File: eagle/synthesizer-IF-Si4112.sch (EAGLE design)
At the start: 34 parts, among them J1 142-0701-851, J3 142-0701-851, U1 SI4112, X1 ECS-TXO-3225

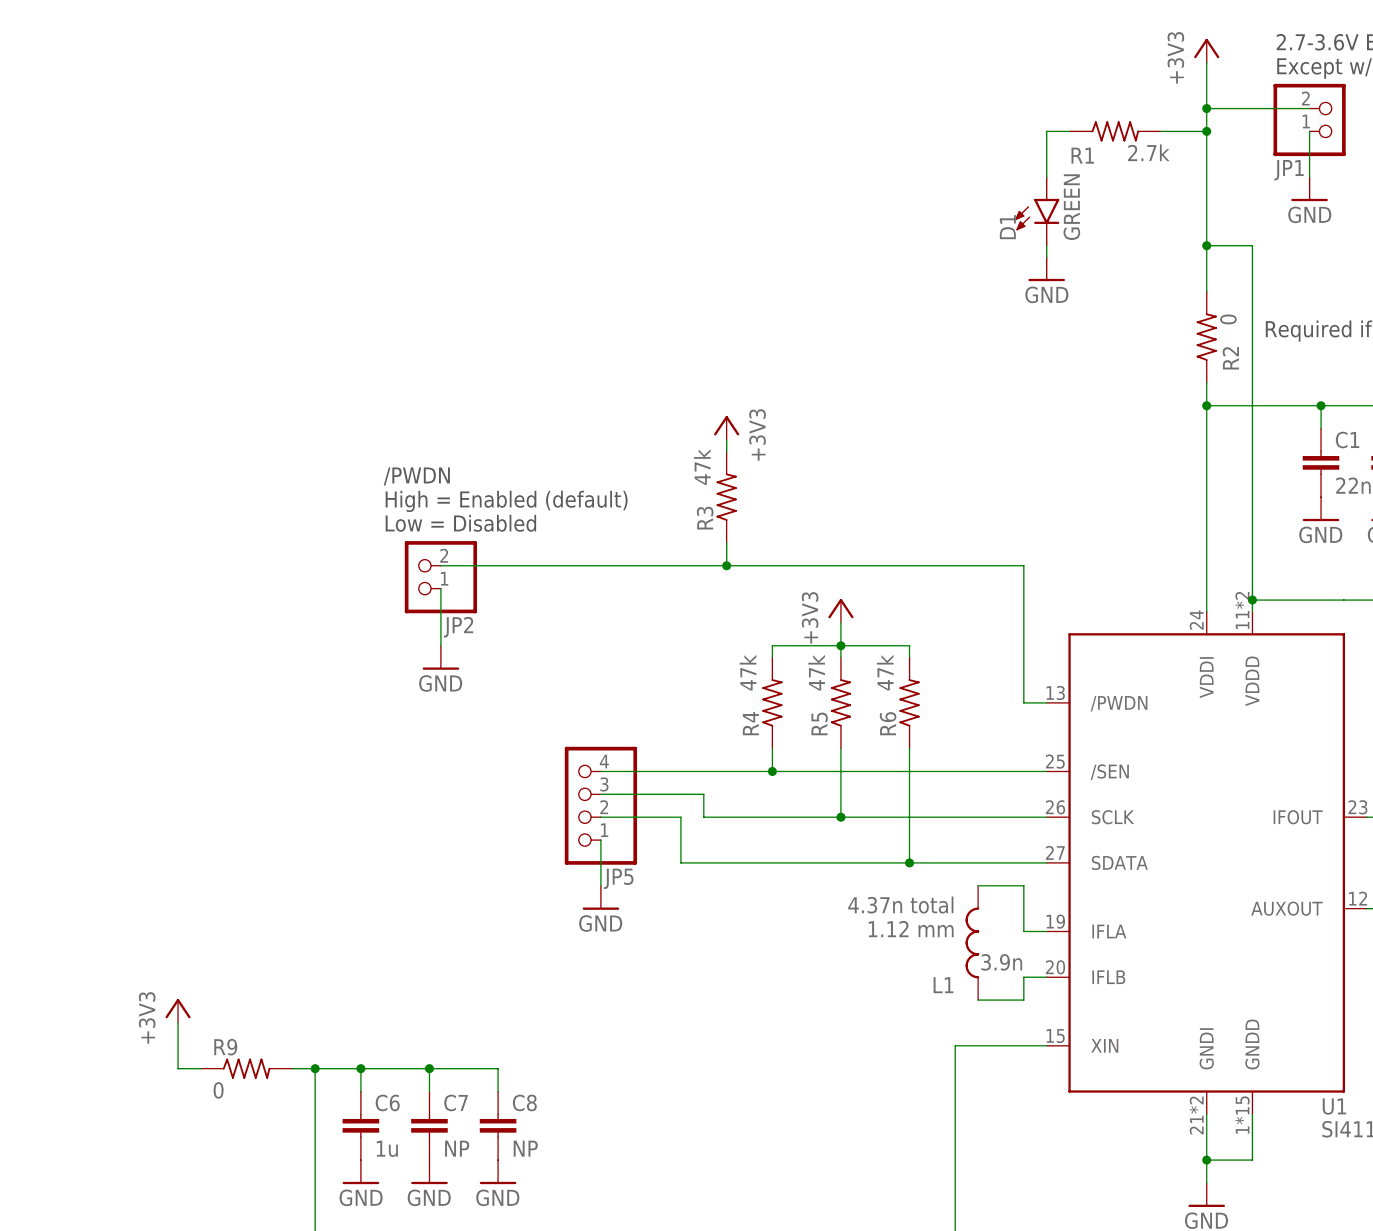
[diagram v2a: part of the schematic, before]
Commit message: Si4112, added better shutdown control
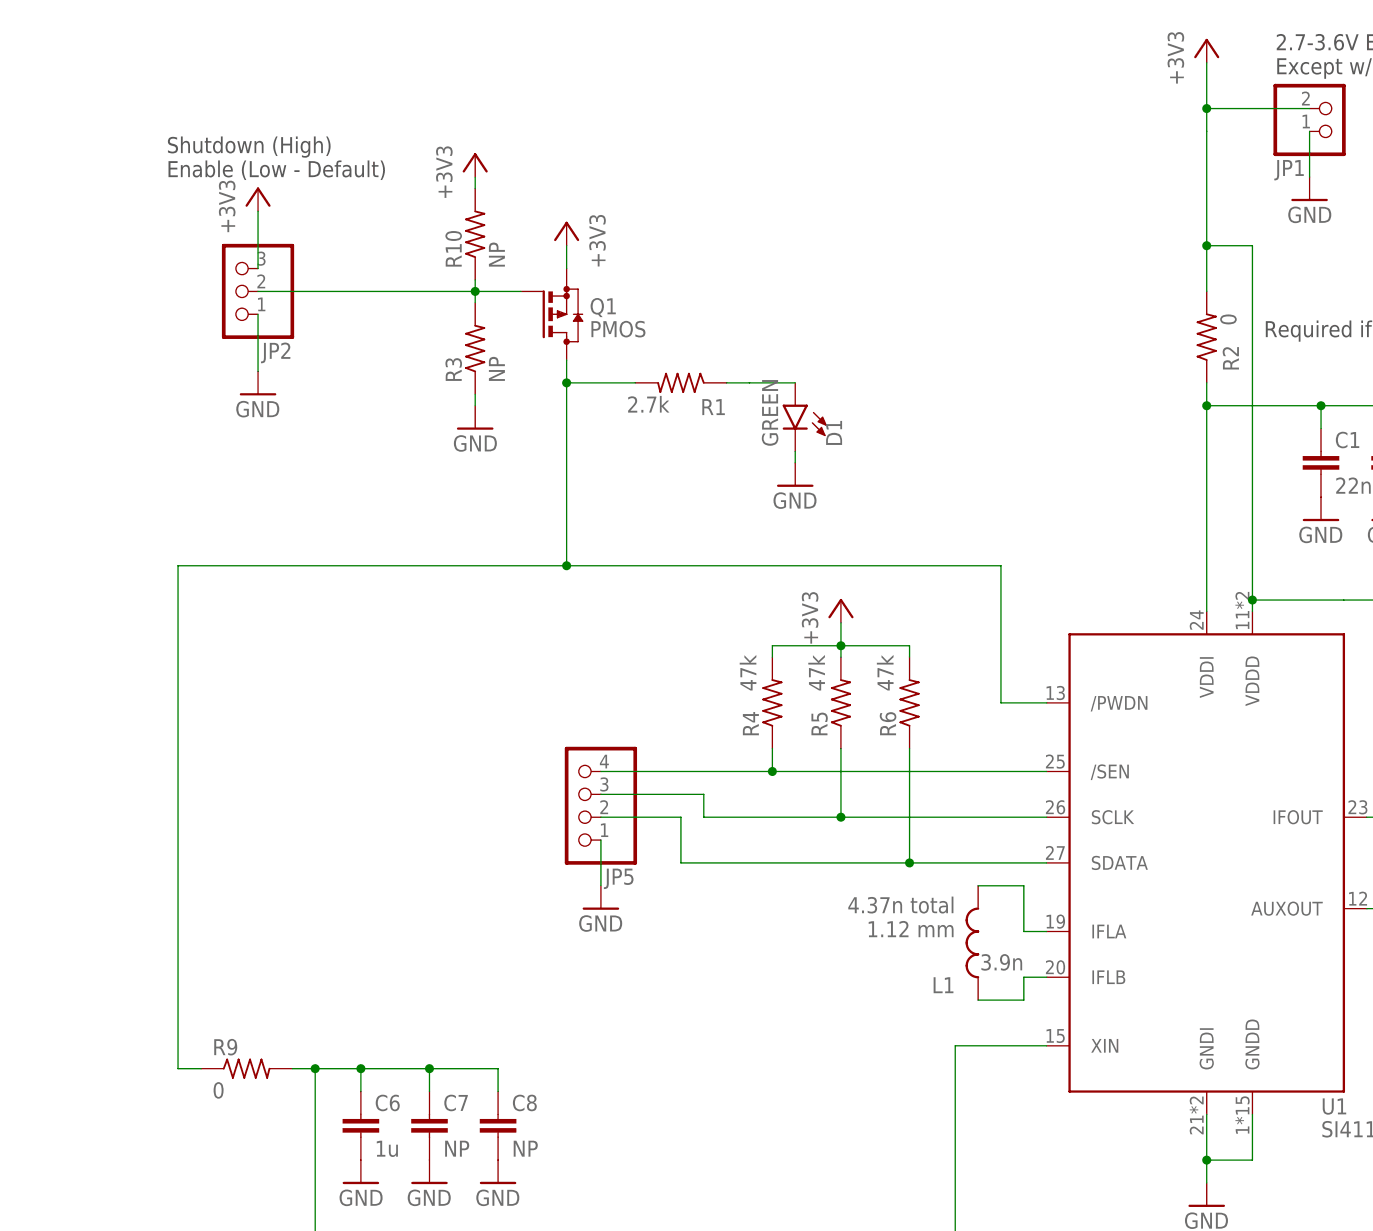
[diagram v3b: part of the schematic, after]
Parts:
- added Q1: PMOS, transistor-small-signal:BSS84
- added R10: NP, oresat-rcl:R-US_0402-B-NOSILK
- JP2: device pinhead:PINHD-1X2 -> pinhead:PINHD-1X3
- R3: value 47k -> NP
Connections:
- removed net /PWDN: JP2.2, R3.1, U1./PWDN
- new net N$4: JP2.2, Q1.G, R10.1, R3.2
- new net N$5: Q1.D, R1.2, R9.1, U1./PWDN
- net +3V3: now also JP2.3, Q1.S, R10.2; no longer R1.2, R3.2, R9.1
- net GND: now also R3.1
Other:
- note added: "Shutdown (High) Enable (Low - Default)"
- note removed: "/PWDN High = Enabled (default) Low = Disabled"
- moved on the sheet: D1, R1, R3

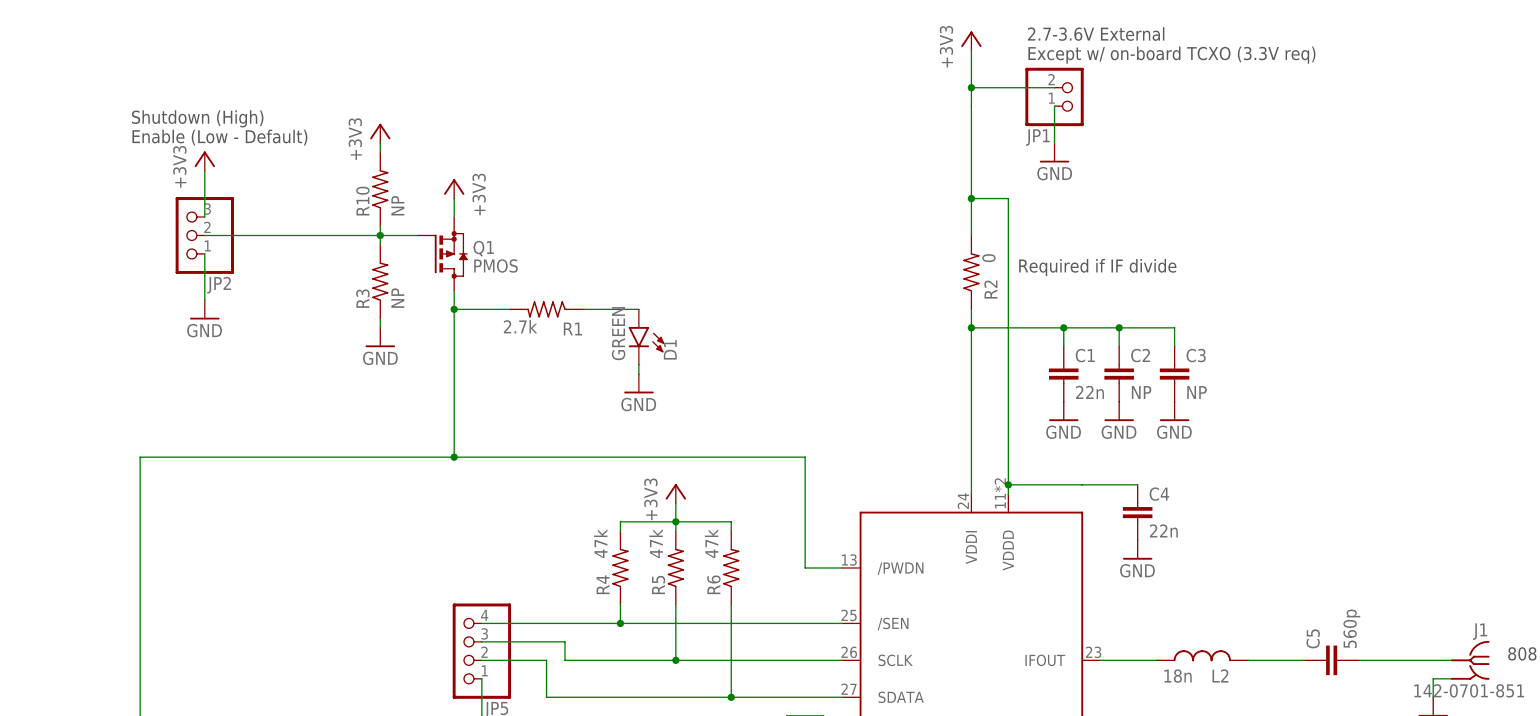
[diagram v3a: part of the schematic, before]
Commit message: Si4112, fix shutdown control and add bkup power down battery option
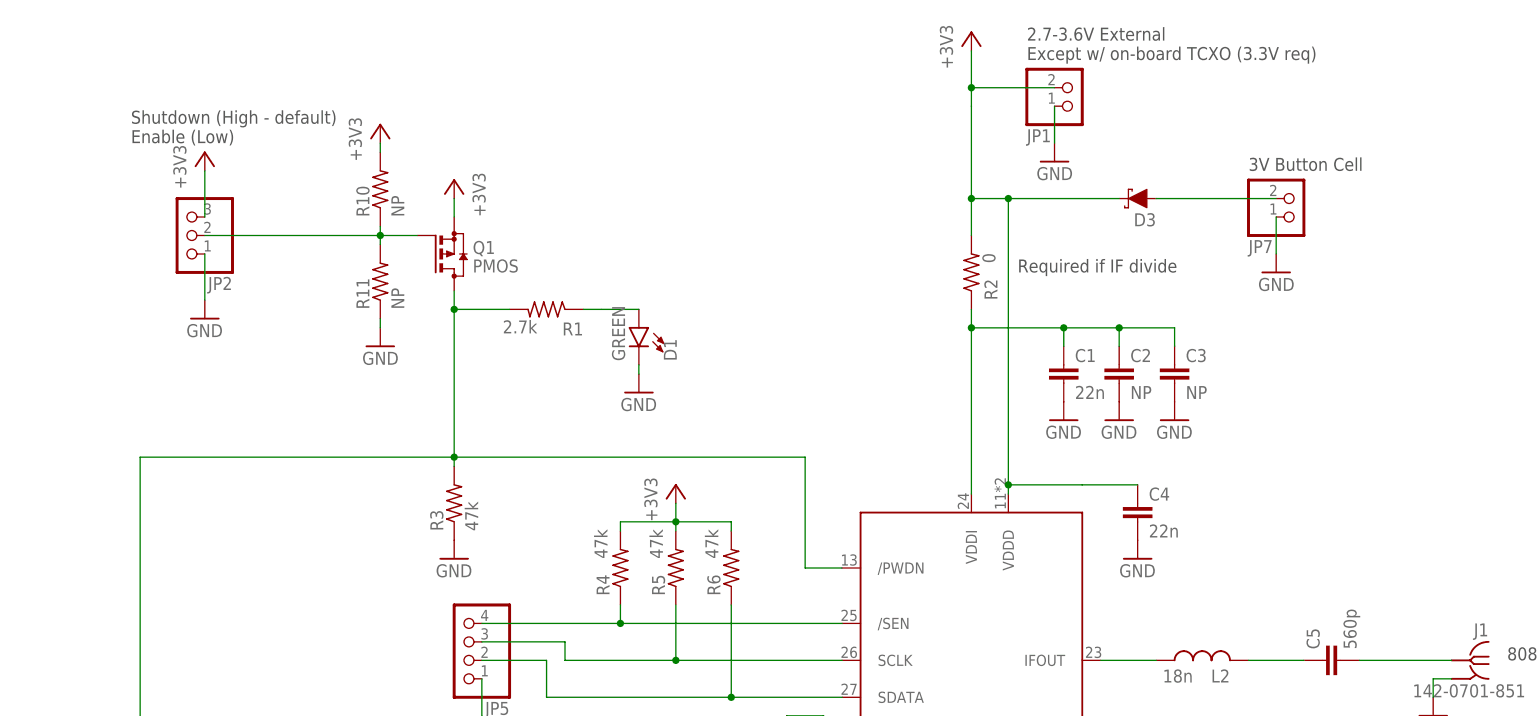
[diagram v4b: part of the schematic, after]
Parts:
- added D3: 120mA/40V/370mV, SparkFun-DiscreteSemi:DIODE-SCHOTTKY-RB751S40
- added JP7: (no value), pinhead:PINHD-1X2
- added R99: NP, oresat-rcl:R-US_0402-B-NOSILK
- R3: value NP -> 47k
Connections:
- new net N$1: D3.A, JP7.2
- net +3V3: now also D3.C
- net GND: now also JP7.1, R11.1
- net N$4: now also R11.2; no longer R3.2
- net N$5: now also R3.2
- net REF_IN: now also R99.2; no longer R11.2
- net XIN: now also R99.1; no longer R11.1
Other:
- note added: "3V Button Cell"
- note added: "Shutdown (High - default) Enable (Low)"
- note removed: "Shutdown (High) Enable (Low - Default)"
- moved on the sheet: R3
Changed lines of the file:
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@@
 <part name="GND13" library="supply1" library_urn="urn:adsk.eagle:library:371" deviceset="GND" device=""/>
 <part name="X1" library="X-ECS-TXO-TCXO" deviceset="ECS-TXO-3225" device=""/>
-<part name="R3" library="oresat-rcl" deviceset="R-US_" device="0402-B-NOSILK" value="NP"/>
+<part name="R11" library="oresat-rcl" deviceset="R-US_" device="0402-B-NOSILK" value="NP"/>
 <part name="GND69" library="supply1" library_urn="urn:adsk.eagle:library:371" deviceset="GND" device=""/>
 <part name="C2" library="oresat-rcl" deviceset="C-EU" device="0603-B-NOSILK" value="NP"/>
@@
 <part name="U1" library="U-Silicon-Labs-Si4133-synthesizer" deviceset="SI4112" device=""/>
 <part name="JP6" library="oresat-rcl" deviceset="R-US_" device="0402-B-NOSILK" value="0"/>
-<part name="R11" library="oresat-rcl" deviceset="R-US_" device="0402-B-NOSILK" value="NP"/>
+<part name="R99" library="oresat-rcl" deviceset="R-US_" device="0402-B-NOSILK" value="NP"/>
 <part name="Q1" library="transistor-small-signal" library_urn="urn:adsk.eagle:library:401" deviceset="BSS84" device="" package3d_urn="urn:adsk.eagle:package:28738/2" value="PMOS"/>
 <part name="+3V1" library="supply1" library_urn="urn:adsk.eagle:library:371" deviceset="+3V3" device=""/>
@@
 <part name="R10" library="oresat-rcl" deviceset="R-US_" device="0402-B-NOSILK" value="NP"/>
 <part name="+3V3" library="supply1" library_urn="urn:adsk.eagle:library:371" deviceset="+3V3" device=""/>
+<part name="JP7" library="pinhead" library_urn="urn:adsk.eagle:library:325" deviceset="PINHD-1X2" device="" package3d_urn="urn:adsk.eagle:package:22435/2"/>
+<part name="GND15" library="supply1" library_urn="urn:adsk.eagle:library:371" deviceset="GND" device=""/>
+<part name="D3" library="SparkFun-DiscreteSemi" library_urn="urn:adsk.eagle:library:514" deviceset="DIODE-SCHOTTKY" device="-RB751S40" package3d_urn="urn:adsk.eagle:package:38442/1" value="120mA/40V/370mV"/>
+<part name="R3" library="oresat-rcl" deviceset="R-US_" device="0402-B-NOSILK" value="47k"/>
+<part name="GND16" library="supply1" deviceset="GND" device=""/>
 </parts>
 <sheets>
@@
 <text x="101.6" y="48.26" size="1.778" layer="97">0402 Jumper
 Cap only required if not CMOS levels</text>
-<text x="34.29" y="175.26" size="1.778" layer="97">Shutdown (High)
-Enable (Low - Default)</text>
+<text x="34.29" y="175.26" size="1.778" layer="97">Shutdown (High - default)
+Enable (Low)</text>
 <text x="17.78" y="49.53" size="1.778" layer="97">TCXO VCTRL
 +/- 5ppm min
@@
 - PLL close to losing lock
 - PLL not locked</text>
+<text x="187.96" y="171.45" size="1.778" layer="97">3V Button Cell</text>
 </plain>
 <instances>
@@
 <attribute name="VALUE" x="64.77" y="36.83" size="1.778" layer="96"/>
 </instance>
-<instance part="R3" gate="R" x="68.58" y="156.21" smashed="yes" rot="R90">
+<instance part="R11" gate="R" x="68.58" y="156.21" smashed="yes" rot="R90">
 <attribute name="NAME" x="67.0814" y="152.4" size="1.778" layer="95" rot="R90"/>
 <attribute name="VALUE" x="71.882" y="152.4" size="1.778" layer="96" rot="R90"/>
@@
 <attribute name="VALUE" x="90.17" y="51.562" size="1.778" layer="96" rot="R180"/>
 </instance>
-<instance part="R11" gate="R" x="96.52" y="48.26" smashed="yes" rot="R270">
+<instance part="R99" gate="R" x="96.52" y="48.26" smashed="yes" rot="R270">
 <attribute name="VALUE" x="98.298" y="46.99" size="1.778" layer="96" rot="R270"/>
 </instance>
@@
 <instance part="+3V3" gate="G$1" x="68.58" y="177.8" smashed="yes">
 <attribute name="VALUE" x="66.04" y="172.72" size="1.778" layer="96" rot="R90"/>
+</instance>
+<instance part="JP7" gate="G$1" x="194.31" y="167.64" smashed="yes" rot="MR180">
+<attribute name="NAME" x="187.96" y="161.925" size="1.778" layer="95" rot="MR180"/>
+<attribute name="VALUE" x="187.96" y="172.72" size="1.778" layer="96" rot="MR180"/>
+</instance>
+<instance part="GND15" gate="1" x="191.77" y="157.48" smashed="yes" rot="MR0">
+<attribute name="VALUE" x="194.31" y="154.94" size="1.778" layer="96" rot="MR0"/>
+</instance>
+<instance part="D3" gate="G$1" x="172.72" y="167.64" smashed="yes" rot="R180">
+<attribute name="NAME" x="175.26" y="165.608" size="1.778" layer="95" font="vector" rot="R180"/>
+</instance>
+<instance part="R3" gate="R" x="78.74" y="125.73" smashed="yes" rot="R90">
+<attribute name="NAME" x="77.2414" y="121.92" size="1.778" layer="95" rot="R90"/>
+<attribute name="VALUE" x="82.042" y="121.92" size="1.778" layer="96" rot="R90"/>
+</instance>
+<instance part="GND16" gate="1" x="78.74" y="118.11" smashed="yes">
+<attribute name="VALUE" x="76.2" y="115.57" size="1.778" layer="96"/>
 </instance>
 </instances>
@@
 </segment>
 <segment>
-<pinref part="R3" gate="R" pin="1"/>
+<pinref part="R11" gate="R" pin="1"/>
 <pinref part="GND11" gate="1" pin="GND"/>
 <wire x1="68.58" y1="151.13" x2="68.58" y2="149.86" width="0.1524" layer="91"/>
+</segment>
+<segment>
+<pinref part="GND15" gate="1" pin="GND"/>
+<pinref part="JP7" gate="G$1" pin="1"/>
+<wire x1="191.77" y1="160.02" x2="191.77" y2="165.1" width="0.1524" layer="91"/>
+</segment>
+<segment>
+<pinref part="R3" gate="R" pin="1"/>
+<pinref part="GND16" gate="1" pin="GND"/>
 </segment>
 </net>
@@
 <pinref part="J3" gate="G$1" pin="RF"/>
 <wire x1="77.47" y1="22.86" x2="96.52" y2="22.86" width="0.1524" layer="91"/>
-<pinref part="R11" gate="R" pin="2"/>
+<pinref part="R99" gate="R" pin="2"/>
 <wire x1="96.52" y1="43.18" x2="96.52" y2="22.86" width="0.1524" layer="91"/>
 </segment>
@@
 <junction x="149.86" y="182.88"/>
 <pinref part="U1" gate="G$1" pin="VDDD"/>
+<pinref part="D3" gate="G$1" pin="C"/>
+<wire x1="154.94" y1="167.64" x2="170.18" y2="167.64" width="0.1524" layer="91"/>
+<junction x="154.94" y="167.64"/>
 </segment>
 <segment>
@@
 <net name="XIN" class="2">
 <segment>
-<pinref part="R11" gate="R" pin="1"/>
+<pinref part="R99" gate="R" pin="1"/>
 <pinref part="JP6" gate="R" pin="1"/>
 <pinref part="U1" gate="G$1" pin="XIN"/>
@@
 <segment>
 <pinref part="Q1" gate="G$1" pin="G"/>
-<pinref part="R3" gate="R" pin="2"/>
+<pinref part="R11" gate="R" pin="2"/>
 <wire x1="73.66" y1="162.56" x2="68.58" y2="162.56" width="0.1524" layer="91"/>
 <wire x1="68.58" y1="162.56" x2="68.58" y2="161.29" width="0.1524" layer="91"/>
@@
 <wire x1="86.36" y1="152.4" x2="78.74" y2="152.4" width="0.1524" layer="91"/>
 <junction x="78.74" y="152.4"/>
-</segment>
-</net>
+<pinref part="R3" gate="R" pin="2"/>
+<wire x1="78.74" y1="130.81" x2="78.74" y2="132.08" width="0.1524" layer="91"/>
+</segment>
+</net>
+<net name="N$1" class="0">
+<segment>
+<pinref part="D3" gate="G$1" pin="A"/>
+<pinref part="JP7" gate="G$1" pin="2"/>
+<wire x1="175.26" y1="167.64" x2="191.77" y2="167.64" width="0.1524" layer="91"/>
+</segment>
+</net>

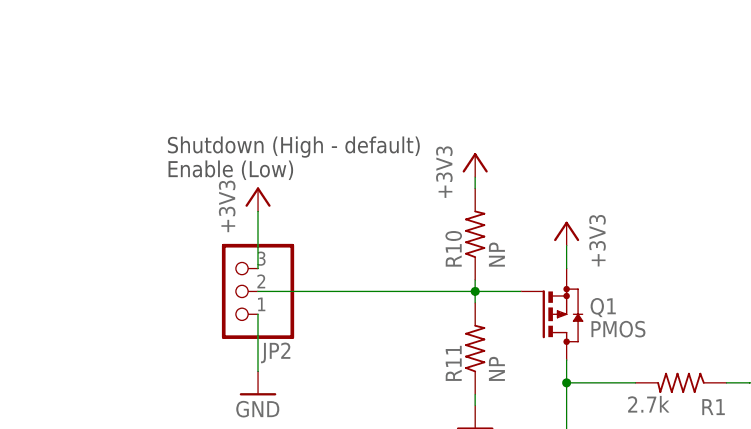
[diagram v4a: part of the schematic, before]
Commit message: Si4112 fix note
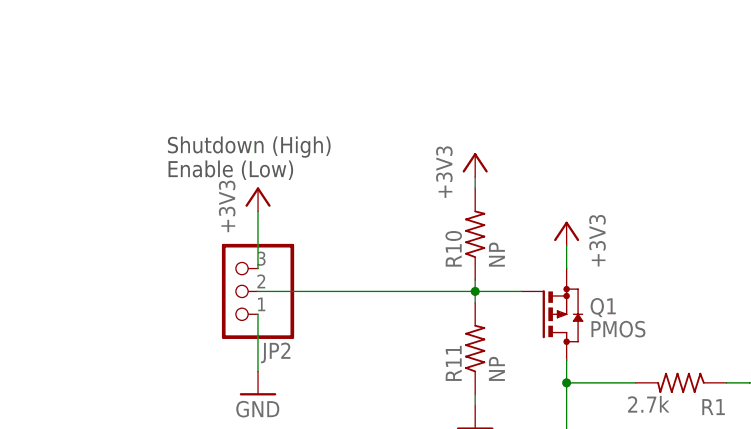
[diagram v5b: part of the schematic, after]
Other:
- note added: "Shutdown (High) Enable (Low)"
- note removed: "Shutdown (High - default) Enable (Low)"
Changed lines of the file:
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@@
 <text x="101.6" y="48.26" size="1.778" layer="97">0402 Jumper
 Cap only required if not CMOS levels</text>
-<text x="34.29" y="175.26" size="1.778" layer="97">Shutdown (High - default)
+<text x="34.29" y="175.26" size="1.778" layer="97">Shutdown (High)
 Enable (Low)</text>
 <text x="17.78" y="49.53" size="1.778" layer="97">TCXO VCTRL
